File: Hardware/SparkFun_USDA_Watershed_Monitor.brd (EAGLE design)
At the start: 63.5 x 63.5 mm, 250 parts, among them J10 QWIIC_RIGHT_ANGLE, J12 3-PIN SMD, J3 QWIIC_RIGHT_ANGLE, J4 U.FL, J5 RJ45, J7 RJ45, J9 RJ45, Q1 20V/4.2A/52mΩ/1.4W, Q10 20V/4.2A/52mΩ/1.4W, Q11 20V/0.2A/8MHz/1.2Ω/1Vth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

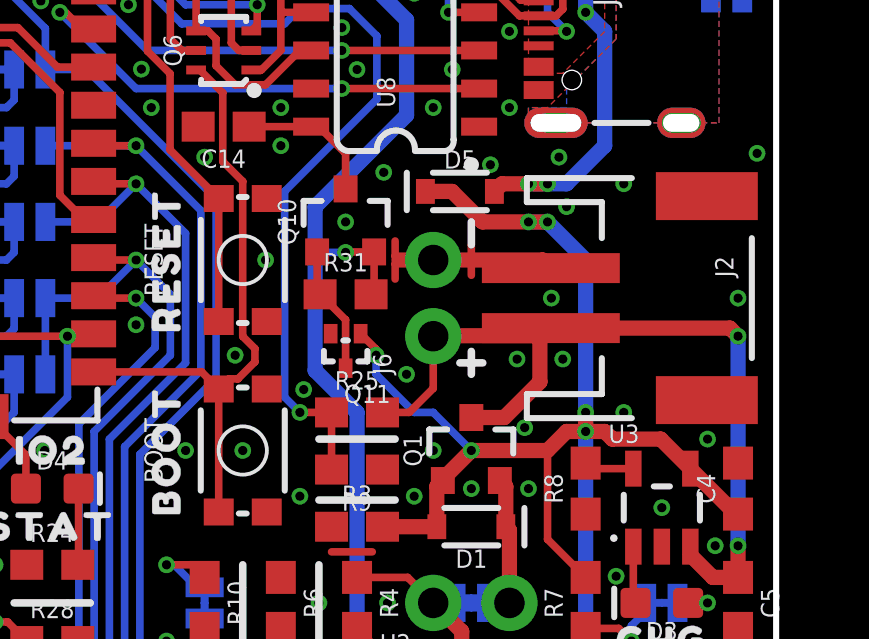
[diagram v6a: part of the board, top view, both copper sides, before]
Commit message: Change CH340 power control to be based on VUSB instead of 5V net
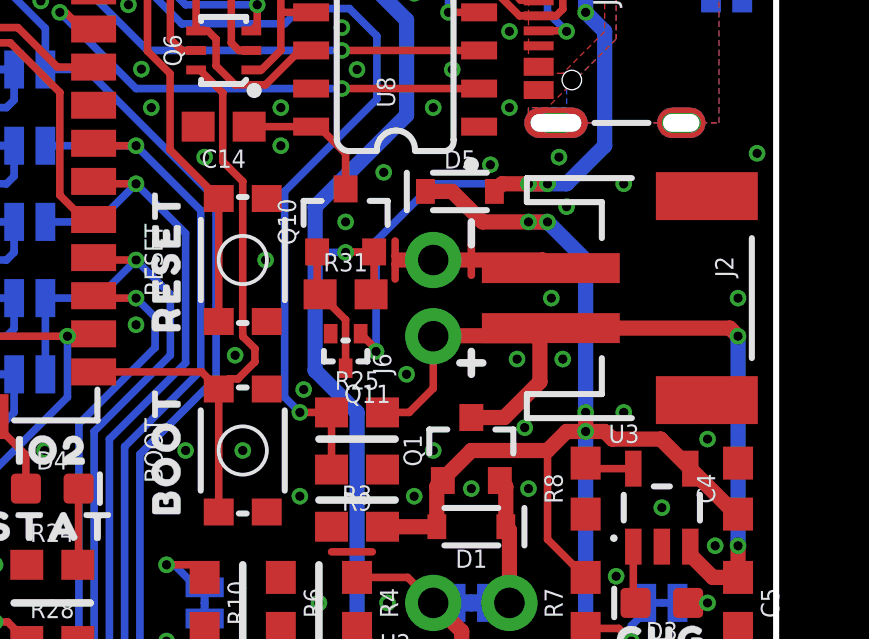
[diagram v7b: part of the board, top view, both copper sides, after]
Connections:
- net 5V: no longer Q11.1
- net V_USB: now also Q11.1
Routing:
- net V_USB: track 10.9 -> 21.3 mm, vias 4 -> 5
- net 5V: track 54.6 -> 48.8 mm, vias 6 -> 4
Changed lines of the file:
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@@
 <wire x1="54.109" y1="45.466" x2="54.363" y2="45.72" width="0.508" layer="1"/>
 <wire x1="54.363" y1="45.72" x2="55.245" y2="45.72" width="0.508" layer="1"/>
+<contactref element="Q11" pad="1"/>
+<wire x1="49.649" y1="40.724" x2="50.165" y2="40.208" width="0.254" layer="1"/>
+<wire x1="50.165" y1="40.208" x2="50.165" y2="40.132" width="0.254" layer="1"/>
+<via x="50.165" y="40.132" extent="1-16" drill="0.3048"/>
+<wire x1="50.165" y1="40.132" x2="50.165" y2="43.815" width="0.254" layer="16"/>
+<wire x1="52.07" y1="45.72" x2="55.245" y2="45.72" width="0.254" layer="16"/>
+<wire x1="50.165" y1="43.815" x2="52.07" y2="45.72" width="0.254" layer="16"/>
 </signal>
 <signal name="5V">
@@
 <wire x1="55.245" y1="44.45" x2="55.88" y2="44.45" width="0.508" layer="1"/>
 <via x="55.88" y="44.45" extent="1-16" drill="0.3048"/>
-<contactref element="Q11" pad="1"/>
 <wire x1="55.245" y1="44.45" x2="53.714" y2="44.45" width="0.508" layer="1"/>
 <wire x1="53.714" y1="44.45" x2="52.698" y2="45.466" width="0.508" layer="1"/>
@@
 <wire x1="57.15" y1="38.1" x2="57.15" y2="43.18" width="0.508" layer="16"/>
 <via x="57.15" y="38.1" extent="1-16" drill="0.3048"/>
-<wire x1="49.649" y1="40.724" x2="50.165" y2="40.208" width="0.254" layer="1"/>
-<wire x1="50.165" y1="40.208" x2="50.165" y2="40.005" width="0.254" layer="1"/>
-<via x="50.165" y="40.005" extent="1-16" drill="0.3048"/>
-<wire x1="50.165" y1="40.005" x2="50.165" y2="39.37" width="0.254" layer="16"/>
-<wire x1="51.435" y1="38.1" x2="52.07" y2="38.1" width="0.254" layer="16"/>
-<wire x1="52.07" y1="38.1" x2="53.34" y2="36.83" width="0.254" layer="16"/>
-<via x="53.34" y="36.83" extent="1-16" drill="0.3048"/>
-<wire x1="50.165" y1="39.37" x2="51.435" y2="38.1" width="0.254" layer="16"/>
 </signal>
 <signal name="N$12">

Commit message: Update RJ45 connector silk
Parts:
- removed U$49, U$63: (no value), output:NC0
- added U$24: (no value), output:3V30
- added U$69: (no value), output:VO0
- moved U$59 3.05 mm to (46.4, 5.71)
- moved U$57 1.52 mm to (46.4, 4.19)
- moved U$58 1.52 mm to (50.2, 5.71)
- moved U$60 1.52 mm to (50.2, 4.19)
- moved U$78 1.52 mm to (46.4, 2.67)
- moved U$25 1.52 mm to (33.7, 2.67)
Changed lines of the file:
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@@
 <element name="U$52" library="output" package="IO250" value="" x="29.845" y="5.715" smashed="yes" rot="MR0"/>
 <element name="U$54" library="output" package="IO330" value="" x="29.845" y="2.667" smashed="yes" rot="MR0"/>
-<element name="U$58" library="output" package="IO170" value="" x="50.165" y="4.191" smashed="yes" rot="MR0"/>
-<element name="U$59" library="output" package="IO180" value="" x="46.355" y="2.667" smashed="yes" rot="MR0"/>
-<element name="U$60" library="output" package="IO190" value="" x="50.165" y="2.667" smashed="yes" rot="MR0"/>
+<element name="U$58" library="output" package="IO170" value="" x="50.165" y="5.715" smashed="yes" rot="MR0"/>
+<element name="U$59" library="output" package="IO180" value="" x="46.355" y="5.715" smashed="yes" rot="MR0"/>
+<element name="U$60" library="output" package="IO190" value="" x="50.165" y="4.191" smashed="yes" rot="MR0"/>
 <element name="U$61" library="output" package="I340" value="" x="33.655" y="4.191" smashed="yes" rot="MR0"/>
 <element name="U$62" library="output" package="I350" value="" x="33.655" y="5.715" smashed="yes" rot="MR0"/>
@@
 <attribute name="VALUE" x="49.53" y="37.338" size="0.6096" layer="27" font="vector" ratio="20" align="top-center"/>
 </element>
-<element name="U$78" library="output" package="IO230" value="" x="46.355" y="4.191" smashed="yes" rot="MR0"/>
+<element name="U$78" library="output" package="IO230" value="" x="46.355" y="2.667" smashed="yes" rot="MR0"/>
 <element name="J8" library="SparkFun-Connectors" package="1X04_NO_SILK" value="" x="62.23" y="13.97" smashed="yes" rot="R270">
 <attribute name="NAME" x="63.627" y="15.24" size="0.6096" layer="25" font="vector" ratio="20" rot="R270"/>
@@
 <attribute name="VALUE" x="21.082" y="53.34" size="0.6096" layer="27" font="vector" ratio="20" rot="R90" align="top-center"/>
 </element>
-<element name="U$49" library="output" package="NC0" value="" x="50.165" y="5.715" smashed="yes" rot="MR0"/>
 <element name="D6" library="SparkFun-DiscreteSemi" package="SOD-323" value="3A/10V/280mV" x="15.24" y="26.67" smashed="yes" rot="R180">
 <attribute name="NAME" x="15.24" y="25.908" size="0.6096" layer="25" font="vector" ratio="20" rot="R180" align="bottom-center"/>
@@
 <attribute name="VALUE" x="41.656" y="14.605" size="0.6096" layer="27" font="vector" ratio="20" rot="R90" align="top-center"/>
 </element>
-<element name="U$57" library="output" package="NC0" value="" x="46.355" y="5.715" smashed="yes" rot="MR0"/>
+<element name="U$57" library="output" package="NC0" value="" x="46.355" y="4.191" smashed="yes" rot="MR0"/>
 <element name="U$117" library="output" package="#5V_IN_#0" value="" x="62.23" y="25.4" smashed="yes"/>
 <element name="U$118" library="output" package="#_5V_IN#0" value="" x="62.23" y="25.4" smashed="yes" rot="MR0"/>
@@
 <attribute name="VALUE" x="3.81" y="32.639" size="0.6096" layer="27" font="vector" ratio="20" rot="R90"/>
 </element>
-<element name="U$63" library="output" package="NC0" value="" x="33.655" y="2.667" smashed="yes" rot="MR0"/>
 <element name="Q8" library="SparkFun-DiscreteSemi" package="SOT-416FL" value="20V/0.2A/8MHz/1.2Ω/1Vth" x="25.4" y="28.829" smashed="yes" rot="R180">
 <attribute name="NAME" x="26.9" y="28.229" size="0.6096" layer="25" font="vector" ratio="20" rot="R180"/>
@@
 <element name="U$88" library="output" package="#GPS#0" value="" x="2.54" y="27.94" smashed="yes"/>
 <element name="U$89" library="output" package="GND3" value="" x="9.525" y="34.29" smashed="yes"/>
-<element name="U$25" library="output" package="VO0" value="" x="33.655" y="1.143" smashed="yes" rot="MR0"/>
+<element name="U$25" library="output" package="VO0" value="" x="33.655" y="2.667" smashed="yes" rot="MR0"/>
 <element name="Q10" library="SparkFun-DiscreteSemi" package="SOT23-3" value="20V/4.2A/52mΩ/1.4W" x="49.149" y="44.45" smashed="yes">
 <attribute name="NAME" x="47.498" y="44.45" size="0.6096" layer="25" font="vector" ratio="20" rot="R90" align="bottom-center"/>
@@
 <element name="U$5" library="output" package="#IO17#0" value="" x="39.497" y="39.37" smashed="yes" rot="MR0"/>
 <element name="U$68" library="output" package="#IO23#0" value="" x="39.497" y="49.53" smashed="yes" rot="MR0"/>
+<element name="U$24" library="output" package="3V30" value="" x="33.655" y="1.143" smashed="yes" rot="MR0"/>
+<element name="U$69" library="output" package="VO0" value="" x="50.165" y="2.667" smashed="yes" rot="MR0"/>
 </elements>
 <signals>
